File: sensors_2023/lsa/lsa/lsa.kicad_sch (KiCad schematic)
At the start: 16 parts, among them J1 Conn_01x07_Male, U1 TCRT5000, U2 TCRT5000, U3 TCRT5000, U4 TCRT5000, U5 TCRT5000

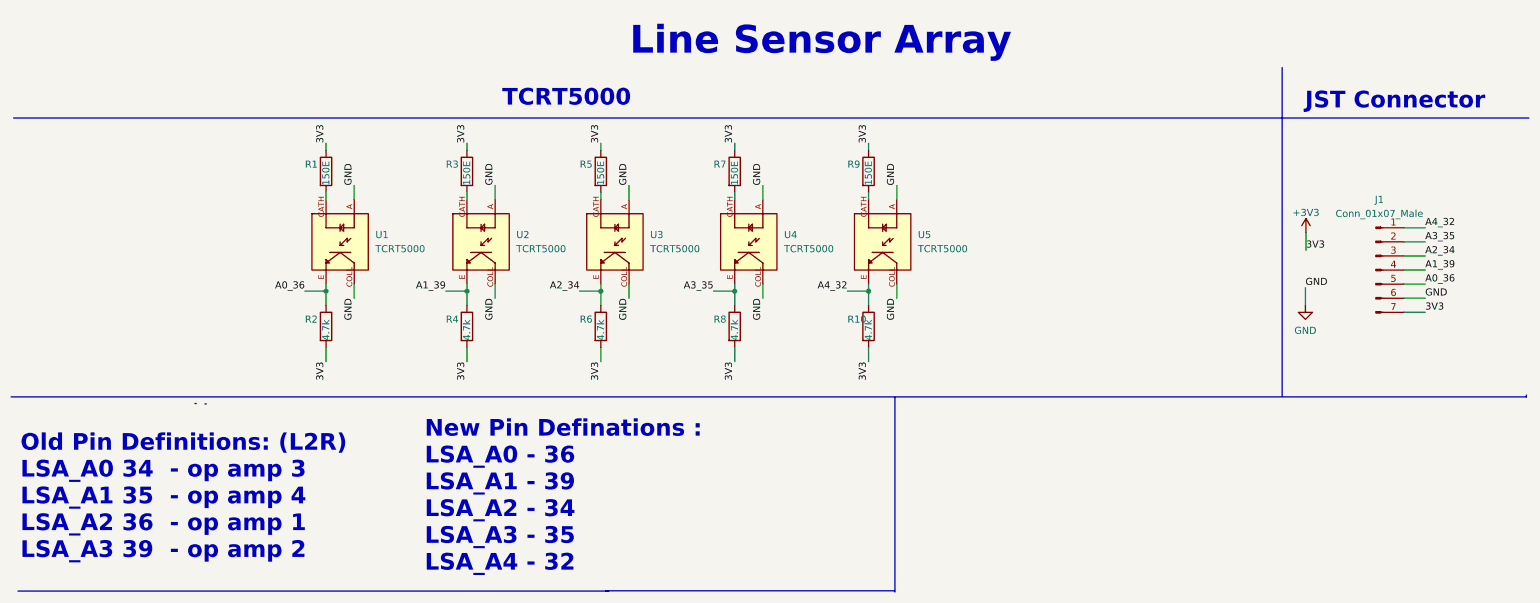
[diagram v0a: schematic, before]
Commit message: Resolve LSA wiring problem and fixed silkscreen, updated gerbers, fabrication outputs and 3D files for LSA
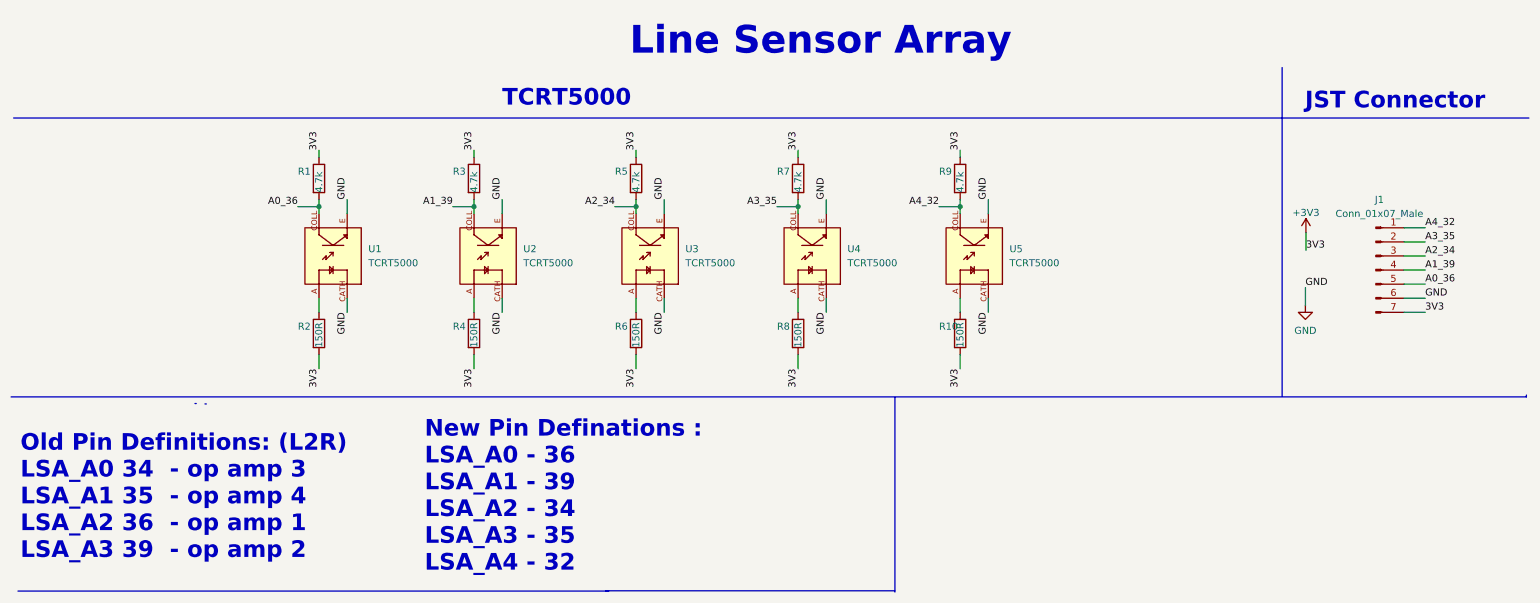
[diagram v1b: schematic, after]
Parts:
- R1, R3, R5, R7, R9: value 150E -> 4.7k
- R10, R2, R4, R6, R8: value 4.7k -> 150R
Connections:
- net A0_36: now also R1.2, U1.COLL; no longer R2.1, U1.E
- net A1_39: now also R3.2, U2.COLL; no longer R4.1, U2.E
- net A2_34: now also R5.2, U3.COLL; no longer R6.1, U3.E
- net A3_35: now also R7.2, U4.COLL; no longer R8.1, U4.E
- net A4_32: now also R9.2, U5.COLL; no longer R10.1, U5.E
- net GND: now also U1.CATH, U1.E, U2.CATH, U2.E, U3.CATH, U3.E, U4.CATH, U4.E, U5.CATH, U5.E; no longer U1.A, U1.COLL, U2.A, U2.COLL, U3.A, U3.COLL, U4.A, U4.COLL, U5.A, U5.COLL
- new net: R10.1, U5.A
- new net: R2.1, U1.A
- new net: R8.1, U4.A
- new net: R6.1, U3.A
- new net: R4.1, U2.A
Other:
- moved on the sheet: R1, R2, U1

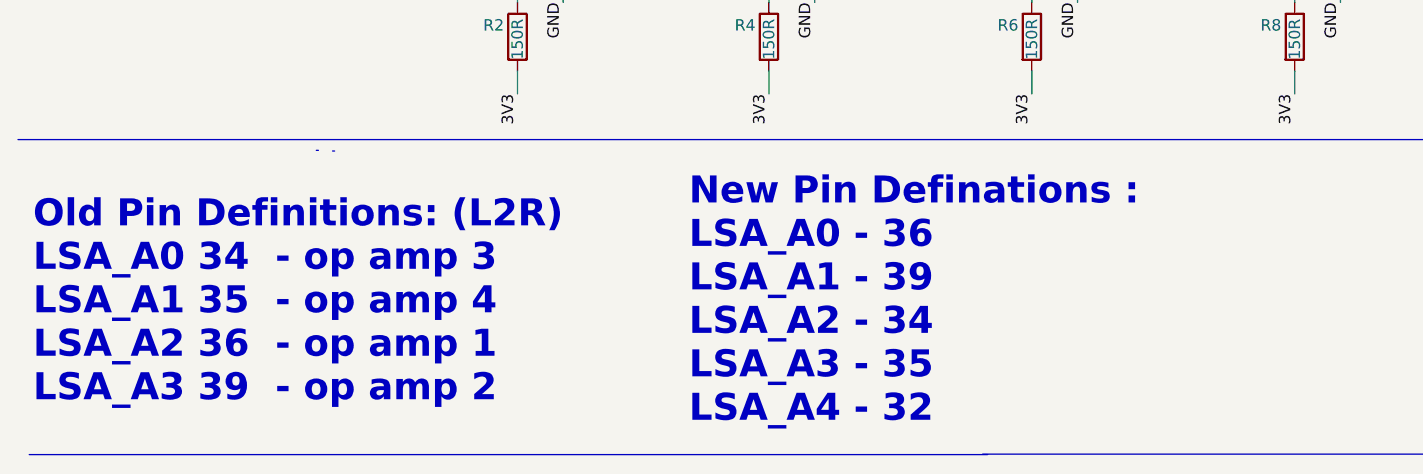
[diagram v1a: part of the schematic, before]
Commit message: Modify relative path for TCRT5000 footprint
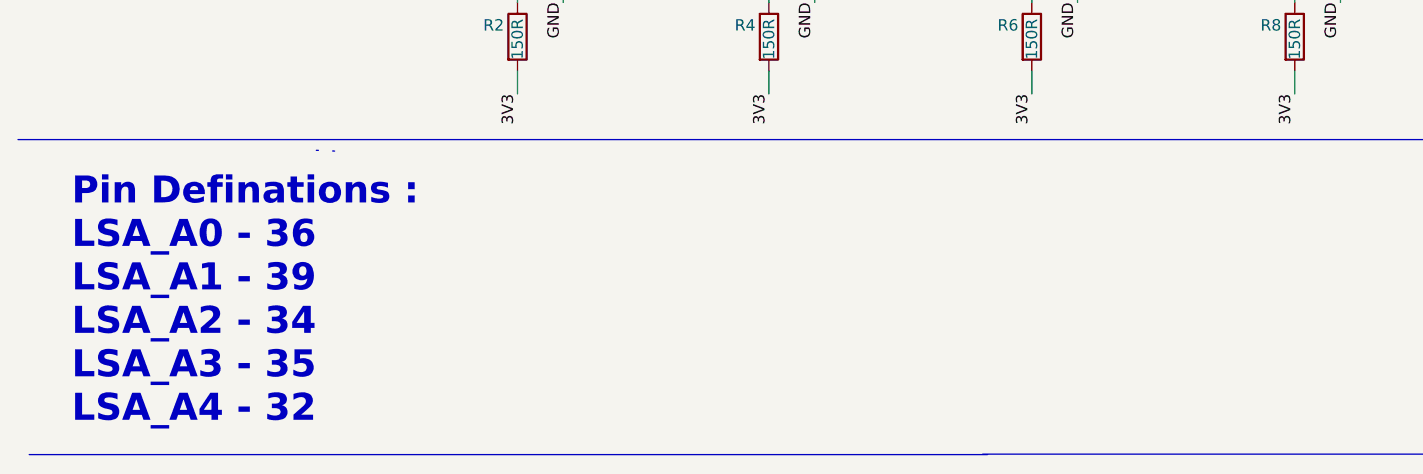
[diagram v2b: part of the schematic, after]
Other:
- note added: "Pin Definations : LSA_A0 - 36 LSA_A1 - 39 LSA_A2 - 34 LSA_A3 - 35 LSA_A4 - 32"
- note removed: "New Pin Definations : LSA_A0 - 36 LSA_A1 - 39 LSA_A2 - 34 LSA_A3 - 35 LSA_A4 - 32"
- note removed: "Old Pin Definitions: (L2R) LSA_A0 34 - op amp 3 LSA_A1 35 - op amp 4 LSA_A2 36 - op amp 1 LSA_A3 39 - op amp 2"
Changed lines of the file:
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@@
-    (effects (font (size 3 3) bold) (justify left bottom))
-  )
-  (text "Old Pin Definitions: (L2R)\nLSA_A0 34  - op amp 3\nLSA_A1 35  - op amp 4\nLSA_A2 36  - op amp 1\nLSA_A3 39  - op amp 2"
-    (at 13.4874 100.584 0)
     (effects (font (size 3 3) bold) (justify left bottom))
   )
@@
     (effects (font (size 3 3) (thickness 0.6) bold) (justify left bottom))
   )
-  (text "New Pin Definations :\nLSA_A0 - 36\nLSA_A1 - 39\nLSA_A2 - 34\nLSA_A3 - 35\nLSA_A4 - 32"
-    (at 86.36 102.87 0)
+  (text "Pin Definations :\nLSA_A0 - 36\nLSA_A1 - 39\nLSA_A2 - 34\nLSA_A3 - 35\nLSA_A4 - 32"
+    (at 17.78 102.87 0)
     (effects (font (size 3 3) (thickness 0.6) bold) (justify left bottom))
   )
